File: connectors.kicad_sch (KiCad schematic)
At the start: 5 parts, among them J1 112-024-113R001, J3 RJHSE5380, J4 USB4085-GF-A

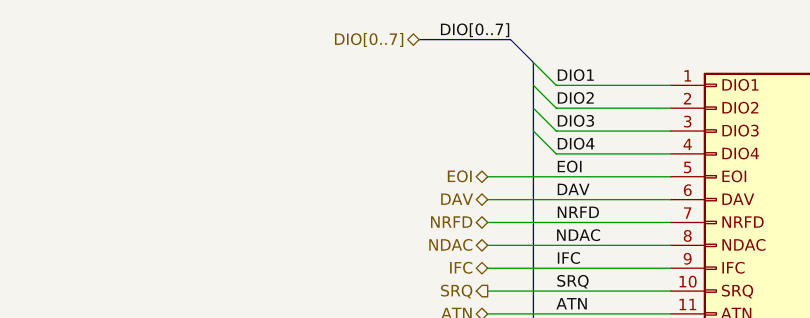
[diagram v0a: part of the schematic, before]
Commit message: Fix GPIB DIO bus nets and start PCB. Adjusted to 4 layers
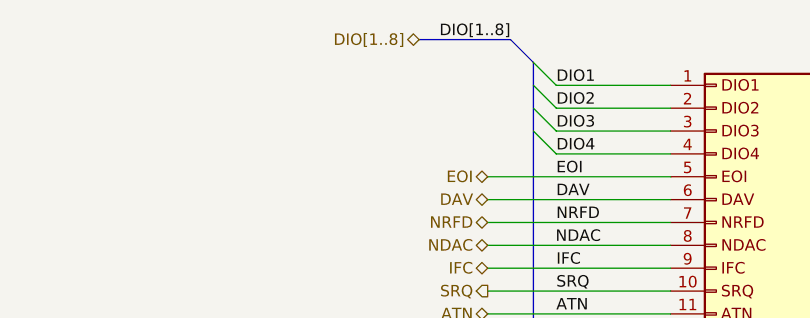
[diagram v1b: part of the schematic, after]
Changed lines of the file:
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@@
 		)
 	)
-	(label "DIO[0..7]"
+	(label "DIO[1..8]"
 		(at 321.31 73.66 180)
 		(effects
@@
 		)
 	)
-	(hierarchical_label "DIO[0..7]"
+	(hierarchical_label "DIO[1..8]"
 		(shape bidirectional)
 		(at 311.15 73.66 180)

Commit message: Update name
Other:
- moved on the sheet: J1, J3, J4, R6, R7
